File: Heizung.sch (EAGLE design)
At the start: 33 parts, among them IC1 MEGA8-PTQFP, Q2 2N7002, Q3 2N7002

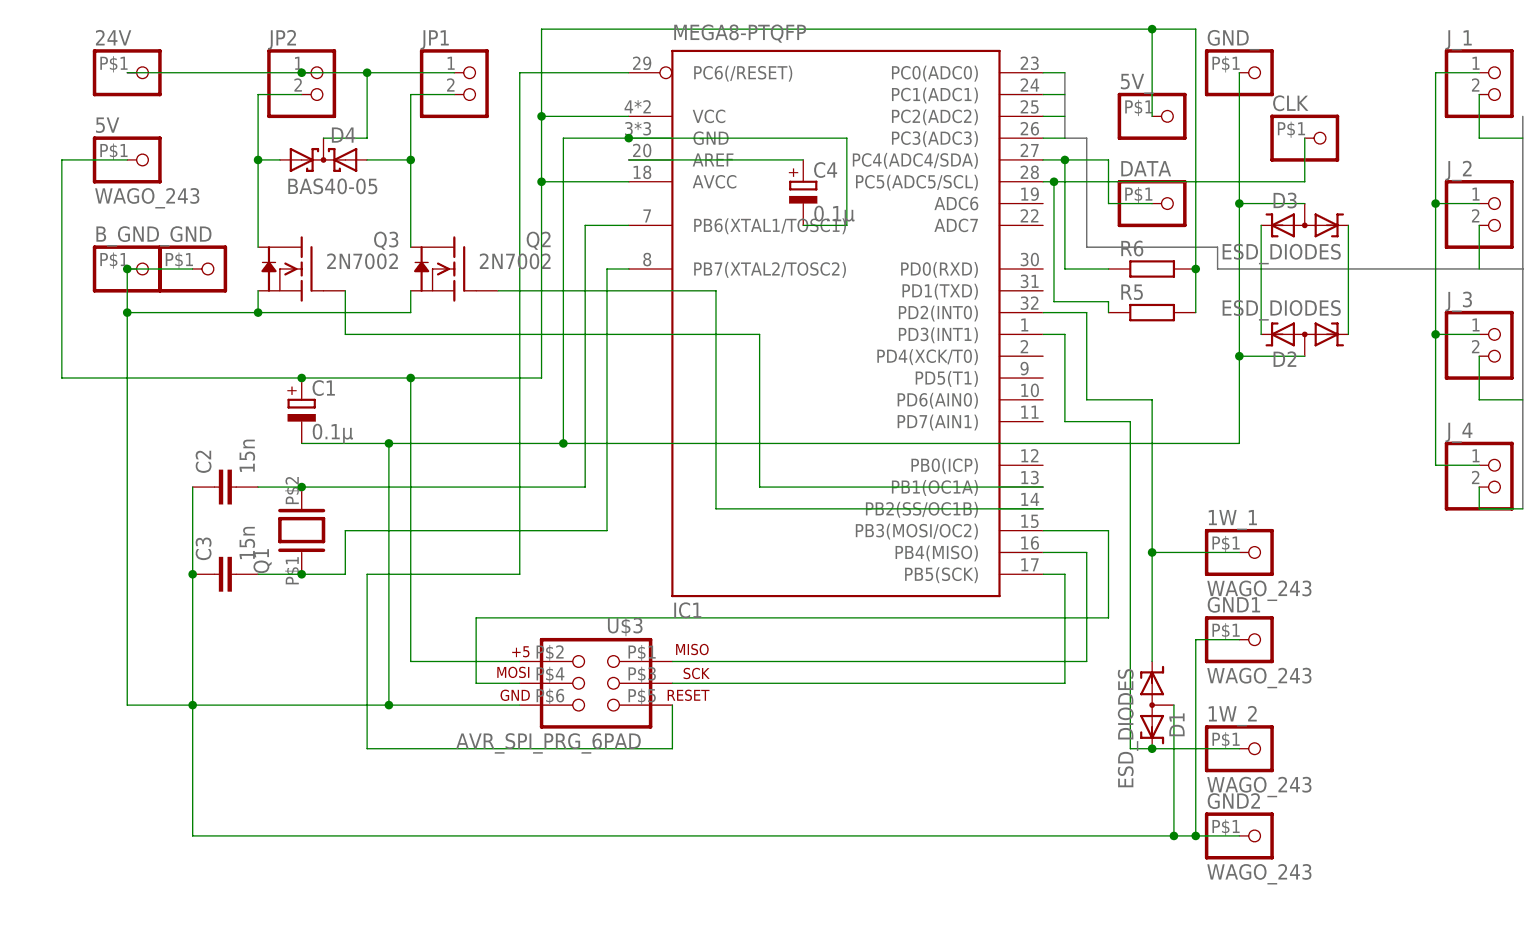
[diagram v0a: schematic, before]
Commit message: v3.0: use separate ground for switched power (24V)
otherwise long cabling will raise ground too much
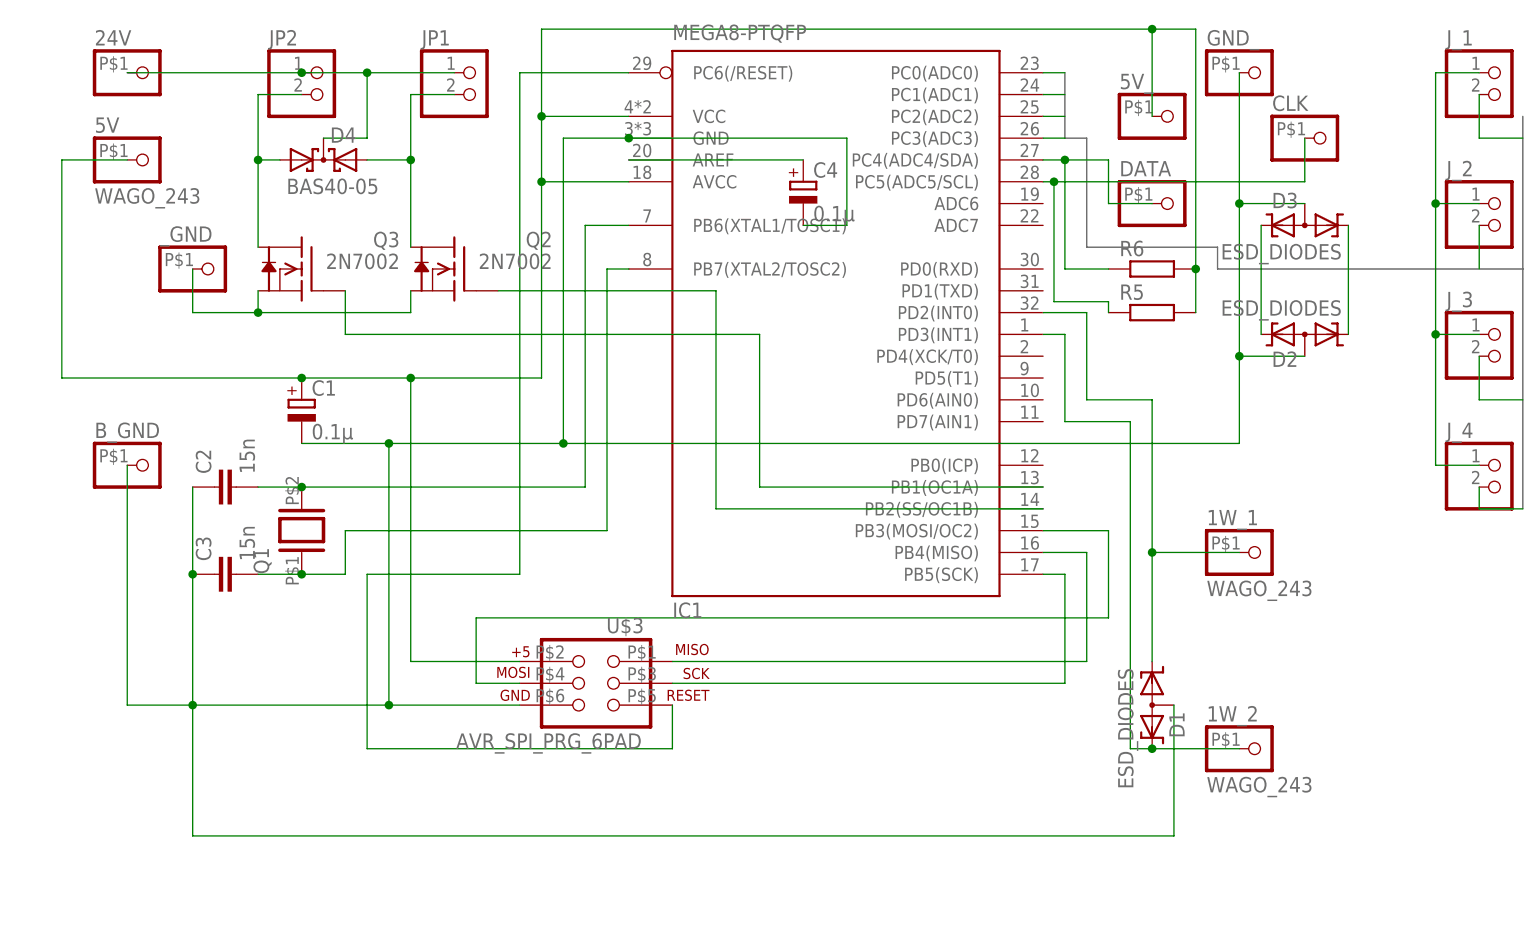
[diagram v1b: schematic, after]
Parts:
- removed GND1, GND2: WAGO_243, common:WAGO_243
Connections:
- new net GND24: Q2.S, Q3.S, _GND.1
- net GND: no longer GND1.1, GND2.1, Q2.S, Q3.S, _GND.1
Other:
- moved on the sheet: B_GND
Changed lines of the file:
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@@
 <?xml version="1.0" encoding="utf-8"?>
 <!DOCTYPE eagle SYSTEM "eagle.dtd">
-<eagle version="7.2.0">
+<eagle version="7.3.0">
 <drawing>
 <settings>
@@
 <part name="5V" library="common" deviceset="WAGO_243" device="" value="WAGO_243"/>
 <part name="1W_1" library="common" deviceset="WAGO_243" device="" value="WAGO_243"/>
-<part name="GND1" library="common" deviceset="WAGO_243" device="" value="WAGO_243"/>
 <part name="1W_2" library="common" deviceset="WAGO_243" device="" value="WAGO_243"/>
-<part name="GND2" library="common" deviceset="WAGO_243" device="" value="WAGO_243"/>
 <part name="5V_" library="common" deviceset="WAGO_243" device="" value="WAGO_243"/>
 <part name="GND_" library="common" deviceset="WAGO_243" device="" value="WAGO_243"/>
@@
 <instance part="C3" gate="G$1" x="25.4" y="63.5" rot="R90"/>
 <instance part="C1" gate="G$1" x="33.02" y="83.82"/>
-<instance part="B_GND" gate="G$1" x="15.24" y="99.06" smashed="yes">
-<attribute name="NAME" x="8.89" y="102.235" size="1.778" layer="95"/>
+<instance part="B_GND" gate="G$1" x="15.24" y="76.2" smashed="yes">
+<attribute name="NAME" x="8.89" y="79.375" size="1.778" layer="95"/>
 </instance>
 <instance part="24V" gate="G$1" x="15.24" y="121.92" smashed="yes">
@@
 <instance part="5V" gate="G$1" x="15.24" y="111.76"/>
 <instance part="1W_1" gate="G$1" x="144.78" y="66.04"/>
-<instance part="GND1" gate="G$1" x="144.78" y="55.88"/>
 <instance part="1W_2" gate="G$1" x="144.78" y="43.18"/>
-<instance part="GND2" gate="G$1" x="144.78" y="33.02"/>
 <instance part="5V_" gate="G$1" x="134.62" y="116.84" smashed="yes">
 <attribute name="NAME" x="128.27" y="120.015" size="1.778" layer="95"/>
@@
 <wire x1="33.02" y1="78.74" x2="43.18" y2="78.74" width="0.1524" layer="91"/>
 <pinref part="B_GND" gate="G$1" pin="1"/>
-<wire x1="12.7" y1="99.06" x2="12.7" y2="93.98" width="0.1524" layer="91"/>
-<wire x1="12.7" y1="93.98" x2="12.7" y2="48.26" width="0.1524" layer="91"/>
+<wire x1="12.7" y1="76.2" x2="12.7" y2="48.26" width="0.1524" layer="91"/>
 <wire x1="12.7" y1="48.26" x2="20.32" y2="48.26" width="0.1524" layer="91"/>
 <junction x="20.32" y="48.26"/>
-<pinref part="Q2" gate="&gt;NAME" pin="S"/>
-<wire x1="45.72" y1="96.52" x2="45.72" y2="93.98" width="0.1524" layer="91"/>
-<wire x1="45.72" y1="93.98" x2="27.94" y2="93.98" width="0.1524" layer="91"/>
-<junction x="12.7" y="93.98"/>
-<wire x1="27.94" y1="93.98" x2="12.7" y2="93.98" width="0.1524" layer="91"/>
 <wire x1="43.18" y1="78.74" x2="63.5" y2="78.74" width="0.1524" layer="91"/>
 <wire x1="63.5" y1="78.74" x2="63.5" y2="114.3" width="0.1524" layer="91"/>
@@
 <pinref part="GND_" gate="G$1" pin="1"/>
 <wire x1="142.24" y1="78.74" x2="142.24" y2="88.9" width="0.1524" layer="91"/>
-<pinref part="GND1" gate="G$1" pin="1"/>
 <wire x1="142.24" y1="88.9" x2="142.24" y2="106.68" width="0.1524" layer="91"/>
 <wire x1="142.24" y1="106.68" x2="142.24" y2="121.92" width="0.1524" layer="91"/>
-<wire x1="137.16" y1="55.88" x2="142.24" y2="55.88" width="0.1524" layer="91"/>
-<pinref part="GND2" gate="G$1" pin="1"/>
-<wire x1="142.24" y1="33.02" x2="137.16" y2="33.02" width="0.1524" layer="91"/>
-<wire x1="137.16" y1="33.02" x2="137.16" y2="55.88" width="0.1524" layer="91"/>
-<wire x1="137.16" y1="33.02" x2="134.62" y2="33.02" width="0.1524" layer="91"/>
 <wire x1="134.62" y1="33.02" x2="20.32" y2="33.02" width="0.1524" layer="91"/>
 <wire x1="20.32" y1="33.02" x2="20.32" y2="48.26" width="0.1524" layer="91"/>
-<junction x="137.16" y="33.02"/>
 <pinref part="D1" gate="G$1" pin="AA"/>
 <wire x1="134.62" y1="48.26" x2="134.62" y2="33.02" width="0.1524" layer="91"/>
-<junction x="134.62" y="33.02"/>
 <pinref part="D2" gate="G$1" pin="AA"/>
 <wire x1="149.86" y1="88.9" x2="142.24" y2="88.9" width="0.1524" layer="91"/>
@@
 <wire x1="149.86" y1="106.68" x2="142.24" y2="106.68" width="0.1524" layer="91"/>
 <junction x="142.24" y="106.68"/>
-<pinref part="Q3" gate="&gt;NAME" pin="S"/>
-<wire x1="27.94" y1="96.52" x2="27.94" y2="93.98" width="0.1524" layer="91"/>
-<junction x="27.94" y="93.98"/>
-<pinref part="_GND" gate="G$1" pin="1"/>
-<wire x1="20.32" y1="99.06" x2="12.7" y2="99.06" width="0.1524" layer="91"/>
-<junction x="12.7" y="99.06"/>
 <wire x1="71.12" y1="114.3" x2="96.52" y2="114.3" width="0.1524" layer="91"/>
 <junction x="71.12" y="114.3"/>
@@
 </segment>
 </net>
+<net name="GND24" class="2">
+<segment>
+<pinref part="Q2" gate="&gt;NAME" pin="S"/>
+<wire x1="45.72" y1="96.52" x2="45.72" y2="93.98" width="0.1524" layer="91"/>
+<wire x1="45.72" y1="93.98" x2="27.94" y2="93.98" width="0.1524" layer="91"/>
+<pinref part="Q3" gate="&gt;NAME" pin="S"/>
+<wire x1="27.94" y1="96.52" x2="27.94" y2="93.98" width="0.1524" layer="91"/>
+<pinref part="_GND" gate="G$1" pin="1"/>
+<wire x1="27.94" y1="93.98" x2="20.32" y2="93.98" width="0.1524" layer="91"/>
+<wire x1="20.32" y1="93.98" x2="20.32" y2="99.06" width="0.1524" layer="91"/>
+<junction x="27.94" y="93.98"/>
+</segment>
+</net>

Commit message: V 3.2: secondary I²C yes, secondary 1wire no
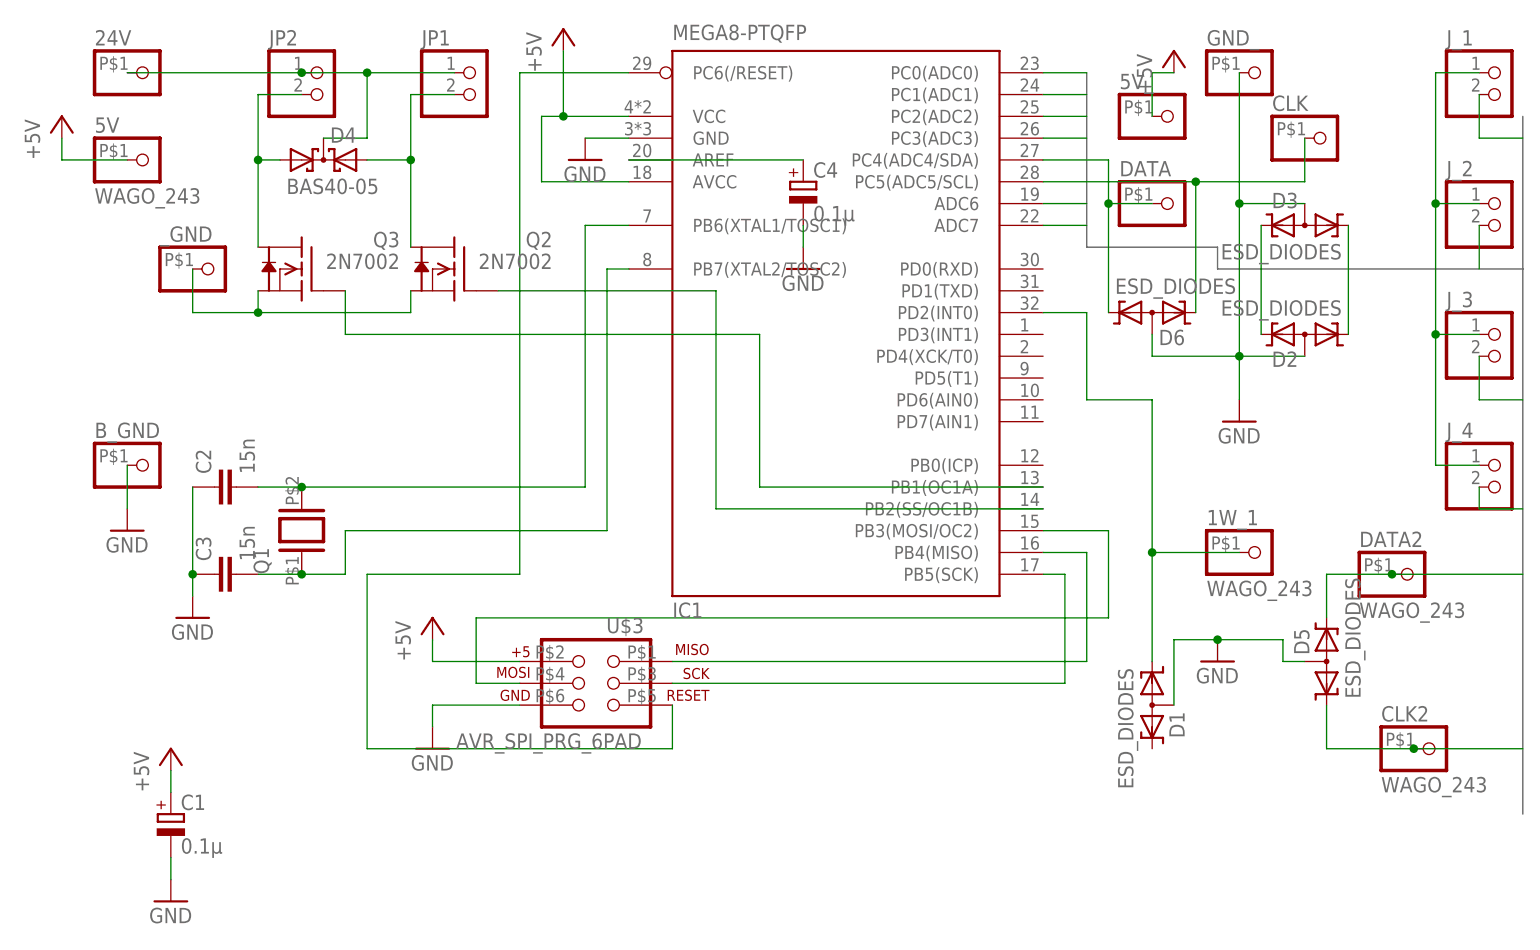
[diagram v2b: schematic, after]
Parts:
- removed 1W_2: WAGO_243, common:WAGO_243
- removed R5, R6: (no value), common:R-EU_M0805
- added CLK2, DATA2: WAGO_243, common:WAGO_243
- added D5, D6: ESD_DIODES, common:ESD_DIODES
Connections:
- removed net 5V: 5V.1, 5V_.1, C1.+, IC1.AVCC, IC1.VCC, R5.2, R6.2, U$3.2
- removed net N$8: 1W_2.1, D1.K2, IC1.PD3(INT1)
- new net +5V: 5V.1, 5V_.1, C1.+, IC1.AVCC, IC1.VCC, U$3.2
- new net B5: D5.K2, DATA2.1, IC1.ADC6
- new net B6: CLK2.1, D5.K1, IC1.ADC7
- net GND: now also D5.AA, D6.AA
- net N$10: now also D6.K1; no longer R6.1
- net N$18: now also D6.K2; no longer R5.1
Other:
- moved on the sheet: C1
